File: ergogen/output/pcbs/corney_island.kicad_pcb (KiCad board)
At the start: 2 copper layers, 134 x 92.5 mm, 46 parts

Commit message: Add additional outputs: images, routed PCB, gerber
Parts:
- D1, D10, D11, D12, D13, D14, D15, D16, D17, D18, D19, D2, D20, D21, D3, D4, D5, D6, D7, D8, D9: value Nexperia_CFP3_SOD-123W -> (none); footprint Diode_SMD:Nexperia_CFP3_SOD-123W -> SmdDiode; moved to F.Cu
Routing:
- net ring_top: vias 0 -> 1
- net ring_home: vias 0 -> 1
- net ring_bottom: vias 0 -> 1
- net pinky_top: vias 0 -> 1
- net pinky_home: vias 0 -> 1
- net pinky_bottom: vias 0 -> 1
- net outer_top: vias 0 -> 1
- net outer_home: vias 0 -> 1
- net outer_bottom: vias 0 -> 1
- net near_home: vias 0 -> 1
- net middle_top: vias 0 -> 1
- net middle_home: vias 0 -> 2
- net middle_bottom: vias 0 -> 1
- net inner_top: vias 0 -> 1
- net inner_home: vias 0 -> 1
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
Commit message: Update outputs with additional plate files
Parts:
- D1, D10, D11, D12, D13, D14, D15, D16, D17, D18, D19, D2, D20, D21, D3, D4, D5, D6, D7, D8, D9: footprint SmdDiode -> ComboDiode
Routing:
- net ring_top: vias 1 -> 0
- net ring_home: vias 1 -> 0
- net ring_bottom: vias 1 -> 0
- net pinky_top: vias 1 -> 0
- net pinky_home: vias 1 -> 0
- net pinky_bottom: vias 1 -> 0
- net outer_top: vias 1 -> 0
- net outer_home: vias 1 -> 0
- net outer_bottom: vias 1 -> 0
- net near_home: vias 1 -> 0
- net middle_top: vias 1 -> 0
- net middle_home: vias 2 -> 0
- net middle_bottom: vias 1 -> 0
- net inner_top: vias 1 -> 0
- net inner_home: vias 1 -> 0
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
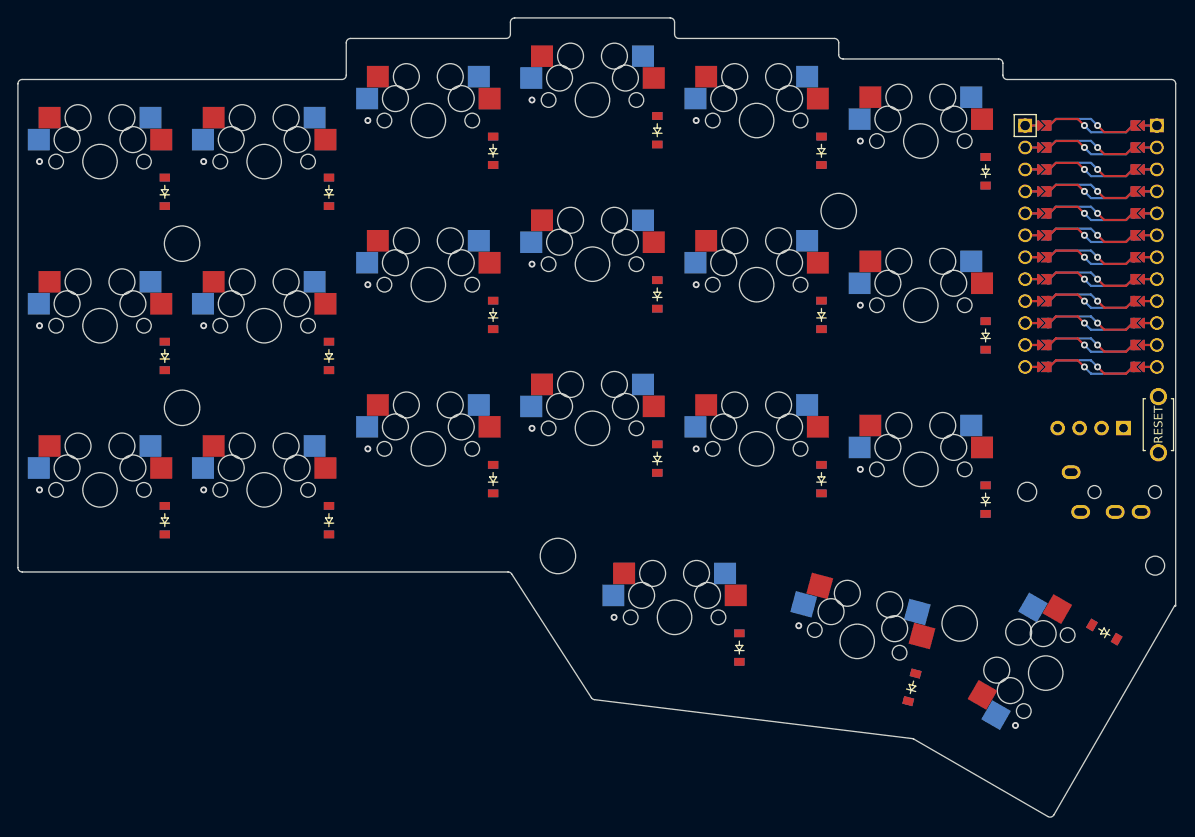
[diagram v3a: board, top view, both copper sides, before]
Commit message: Add LED cutouts
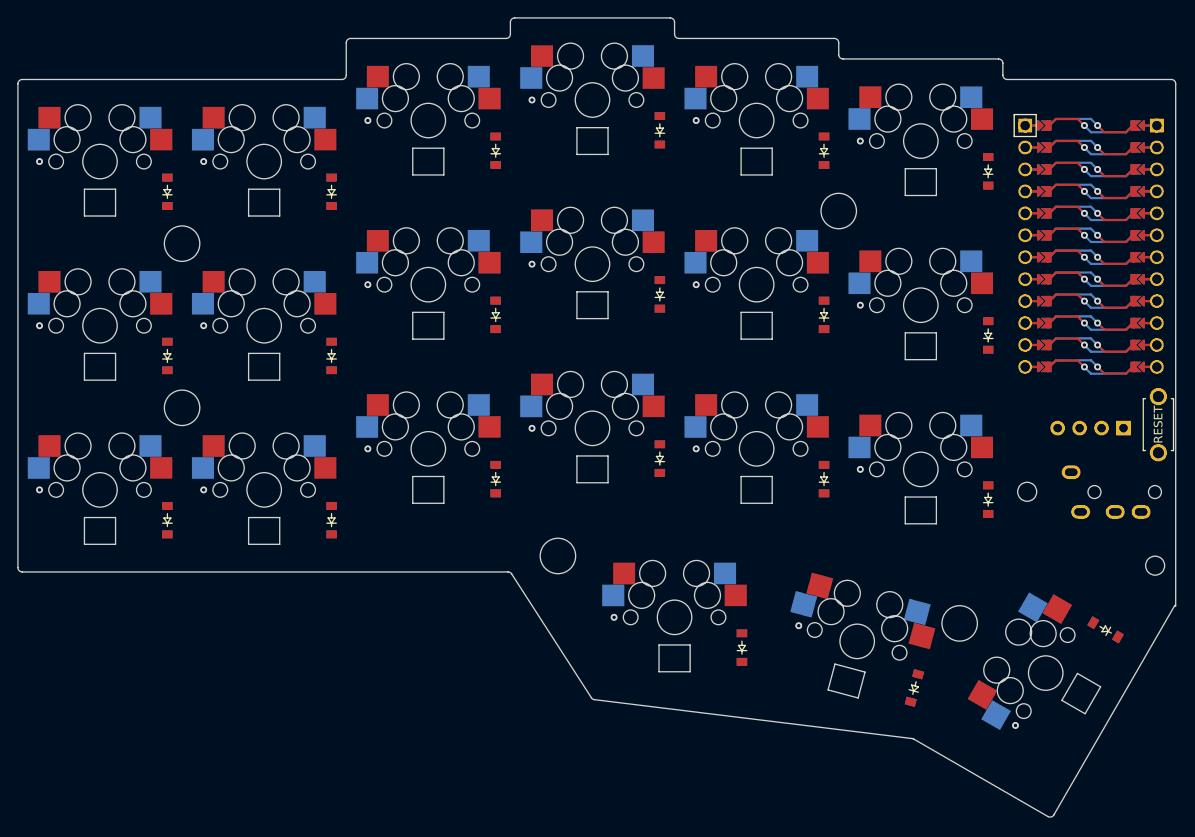
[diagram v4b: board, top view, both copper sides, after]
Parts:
- moved D20 0.30 mm to (194.3, 122.9)
- moved D10 0.30 mm to (164.8, 96.4)
- moved D11 0.30 mm to (164.8, 77.4)
- moved D12 0.30 mm to (164.8, 58.4)
- moved D13 0.30 mm to (183.8, 98.8)
- moved D14 0.30 mm to (183.8, 79.8)
- moved D15 0.30 mm to (183.8, 60.8)
- moved D16 0.30 mm to (202.8, 101.1)
- moved D17 0.30 mm to (202.8, 82.1)
- moved D18 0.30 mm to (202.8, 63.1)
- moved D19 0.30 mm to (174.3, 118.2)
- moved D7 0.30 mm to (145.8, 98.8)
- moved D8 0.30 mm to (145.8, 79.8)
- moved D9 0.30 mm to (145.8, 60.8)
- moved D1 0.30 mm to (107.8, 103.5)
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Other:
- outline, holes or cut-outs redrawn

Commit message: Fix key positions to exactly match the corne
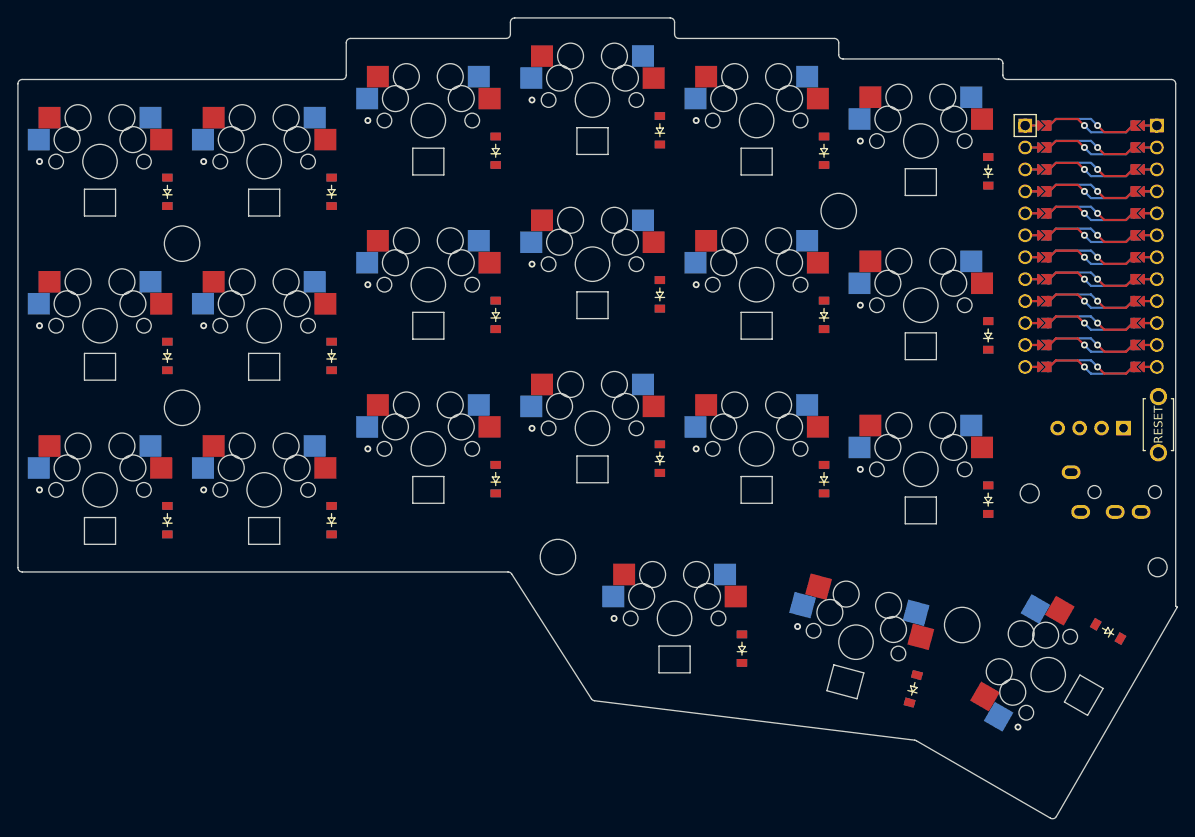
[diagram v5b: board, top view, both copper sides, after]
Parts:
- moved D21 0.34 mm to (216.7, 116.4)
- moved S21 0.34 mm to (209.7, 121.4)
- moved D20 0.16 mm to (194.1, 123.0)
- moved S20 0.16 mm to (187.5, 117.6)
- moved D19 0.12 mm to (174.3, 118.4)
- moved S19 0.12 mm to (166.5, 114.9)
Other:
- board size 134 x 92.5 mm -> 134.2 x 92.7 mm

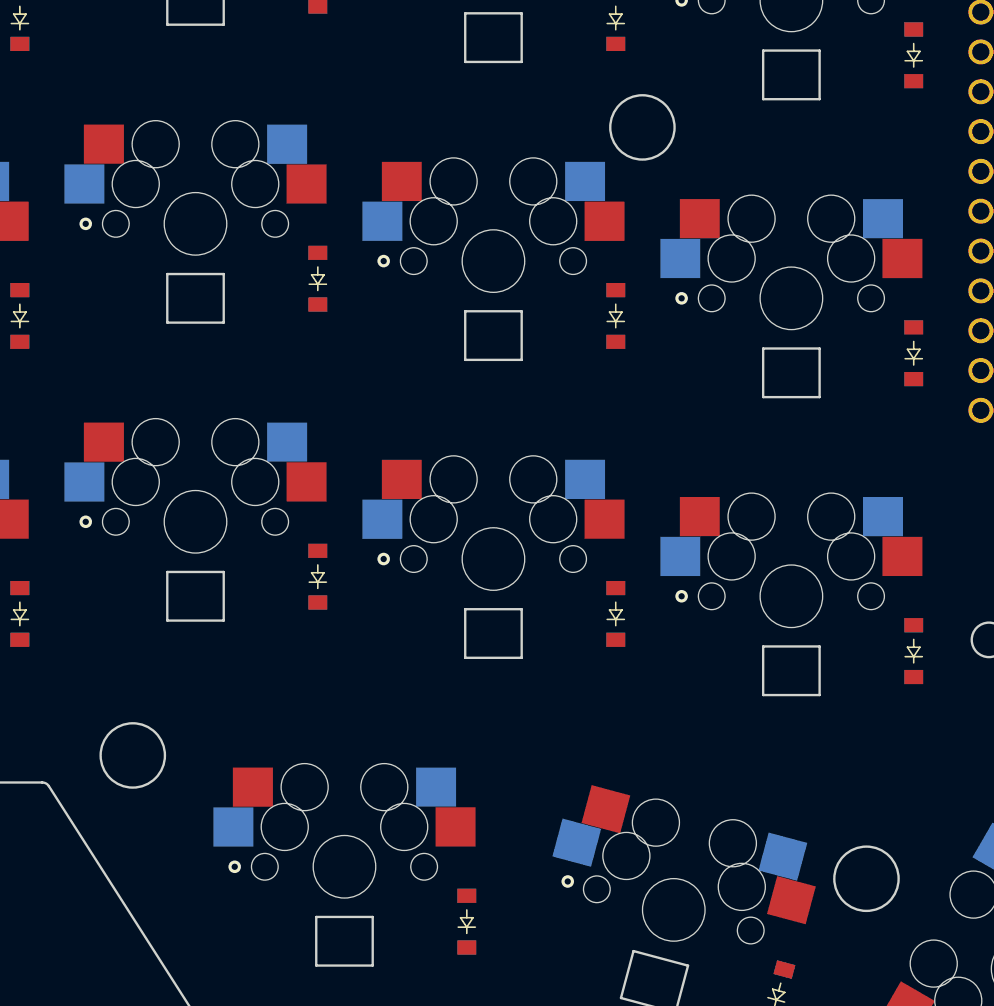
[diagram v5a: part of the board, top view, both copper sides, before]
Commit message: Fix screw spacer holes to match the corne
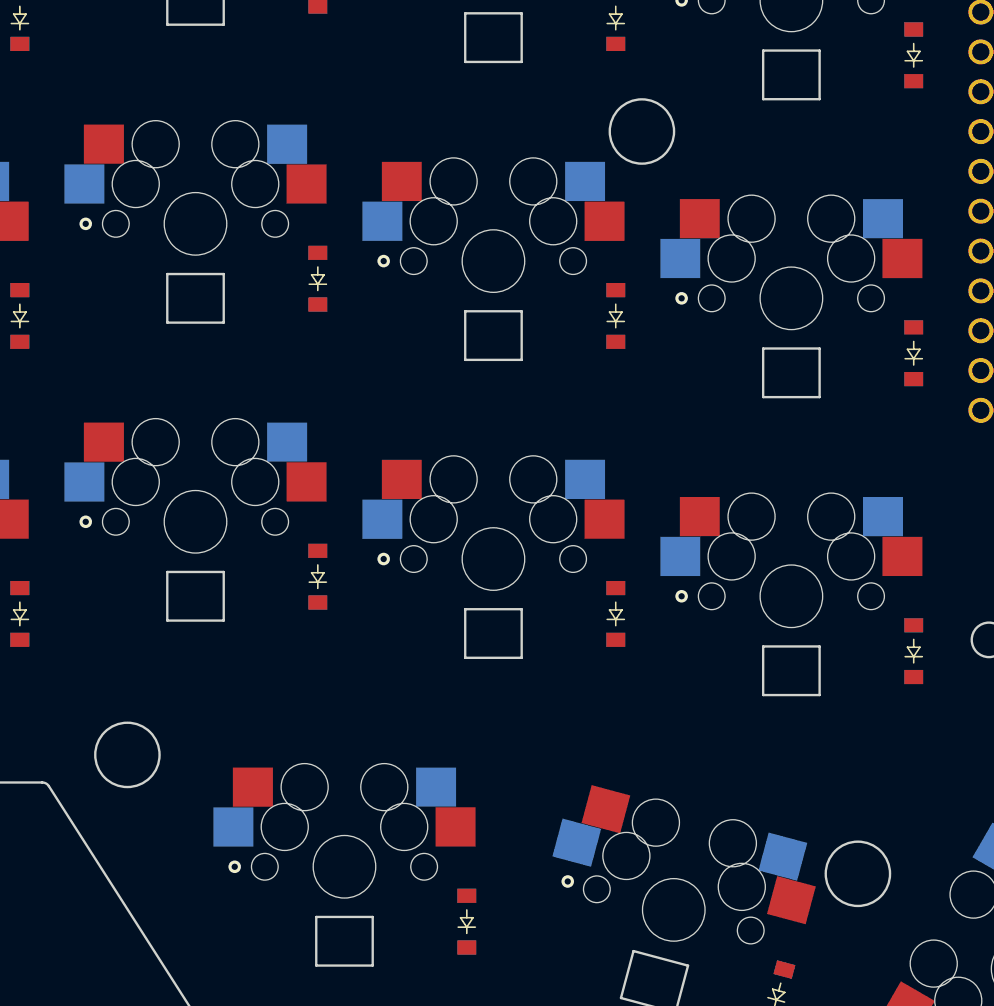
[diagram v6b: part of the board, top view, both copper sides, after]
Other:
- outline, holes or cut-outs redrawn
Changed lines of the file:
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@@
 (gr_circle (center 109.5 71.5) (end 111.55 71.5) (layer Edge.Cuts) (width 0.15))
 (gr_circle (center 109.5 90.5) (end 111.55 90.5) (layer Edge.Cuts) (width 0.15))
-(gr_circle (center 185.5 67.725) (end 187.55 67.725) (layer Edge.Cuts) (width 0.15))
-(gr_circle (center 153 107.775) (end 155.05 107.775) (layer Edge.Cuts) (width 0.15))
-(gr_circle (center 199.7875137 115.6391576) (end 201.83751370000002 115.6391576) (layer Edge.Cuts) (width 0.15))
+(gr_circle (center 185.468 67.986) (end 187.518 67.986) (layer Edge.Cuts) (width 0.15))
+(gr_circle (center 152.657 107.74) (end 154.70700000000002 107.74) (layer Edge.Cuts) (width 0.15))
+(gr_circle (center 199.2410516 115.3236576) (end 201.2910516 115.3236576) (layer Edge.Cuts) (width 0.15))
 (gr_circle (center 207.6013921 100.4051232) (end 208.7013921 100.4051232) (layer Edge.Cuts) (width 0.15))
 (gr_circle (center 222.4104265 108.9551232) (end 223.5104265 108.9551232) (layer Edge.Cuts) (width 0.15))

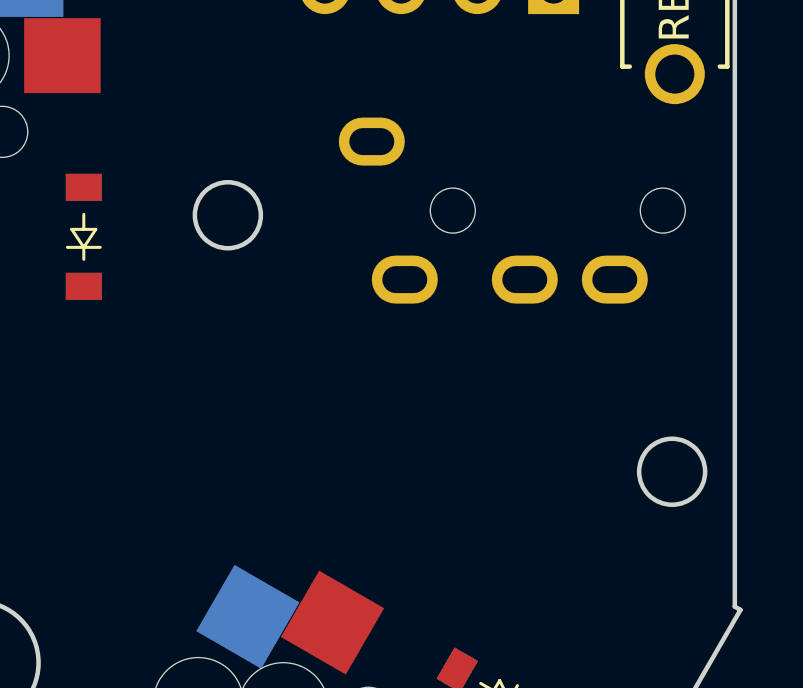
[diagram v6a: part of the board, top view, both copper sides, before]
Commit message: Fix MCU cover mounting holes position
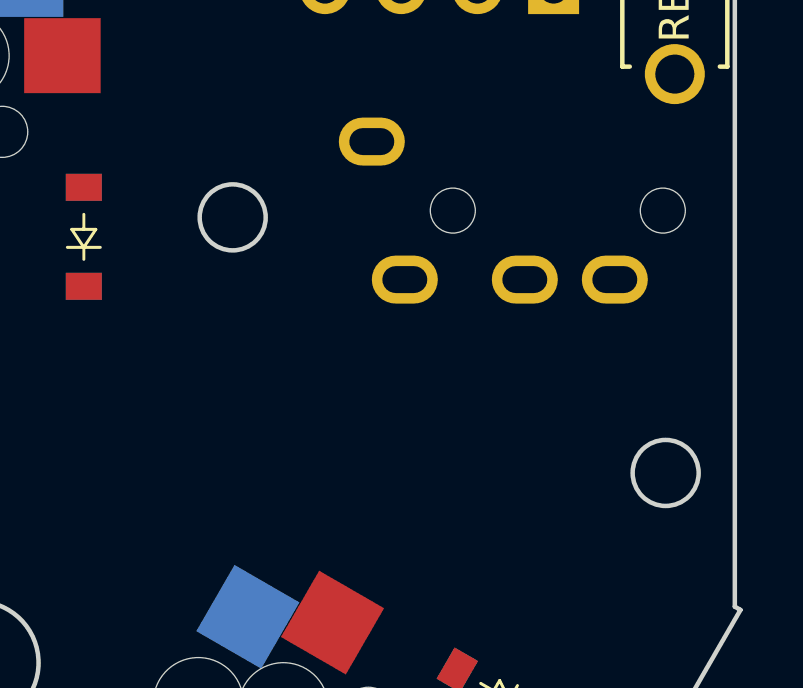
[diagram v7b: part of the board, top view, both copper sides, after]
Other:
- outline, holes or cut-outs redrawn
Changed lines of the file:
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@@
 (gr_circle (center 152.657 107.74) (end 154.70700000000002 107.74) (layer Edge.Cuts) (width 0.15))
 (gr_circle (center 199.2410516 115.3236576) (end 201.2910516 115.3236576) (layer Edge.Cuts) (width 0.15))
-(gr_circle (center 207.6013921 100.4051232) (end 208.7013921 100.4051232) (layer Edge.Cuts) (width 0.15))
-(gr_circle (center 222.4104265 108.9551232) (end 223.5104265 108.9551232) (layer Edge.Cuts) (width 0.15))
+(gr_circle (center 207.762 100.476) (end 208.862 100.476) (layer Edge.Cuts) (width 0.15))
+(gr_circle (center 222.194 108.995) (end 223.29399999999998 108.995) (layer Edge.Cuts) (width 0.15))
 (gr_line (start 98.2 106.3) (end 101.8 106.3) (angle 90) (layer Edge.Cuts) (width 0.15))
 (gr_line (start 101.8 106.3) (end 101.8 103.2) (angle 90) (layer Edge.Cuts) (width 0.15))

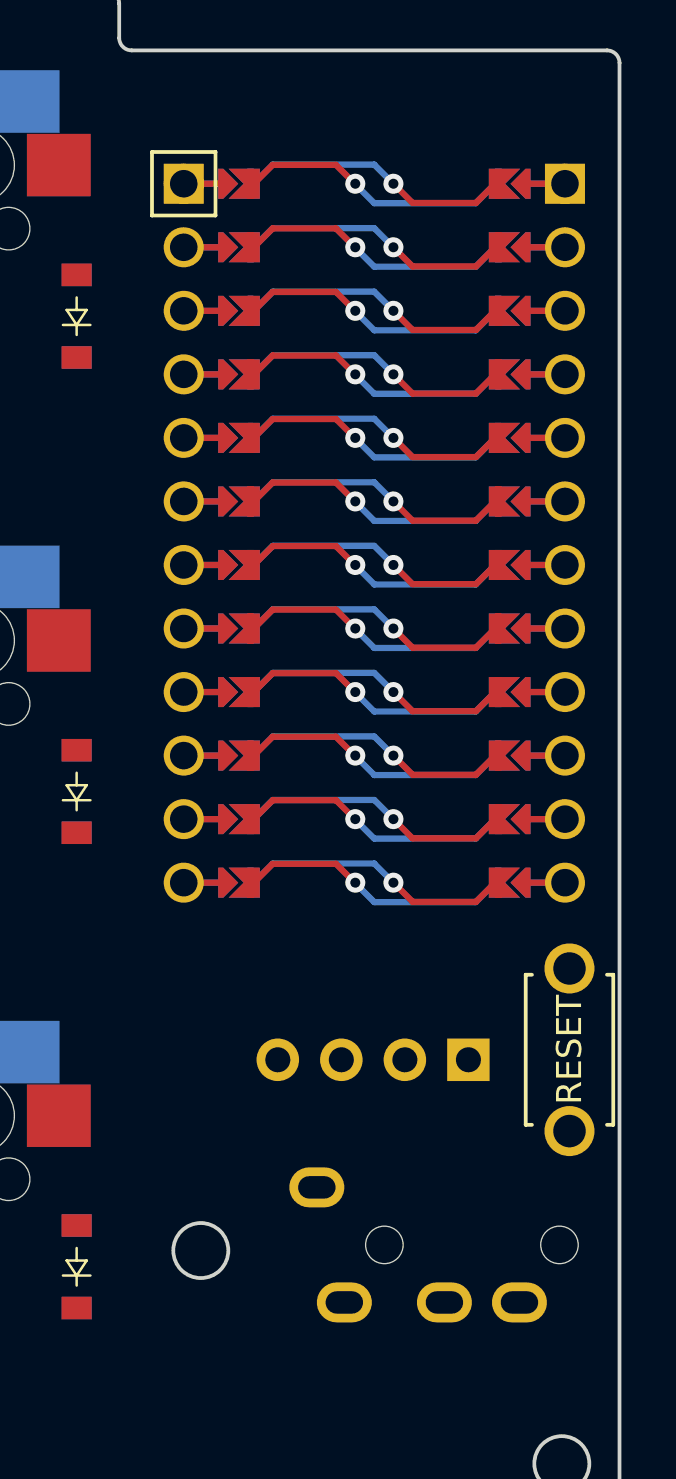
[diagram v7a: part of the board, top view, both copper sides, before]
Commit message: Fix component positions to match the corne
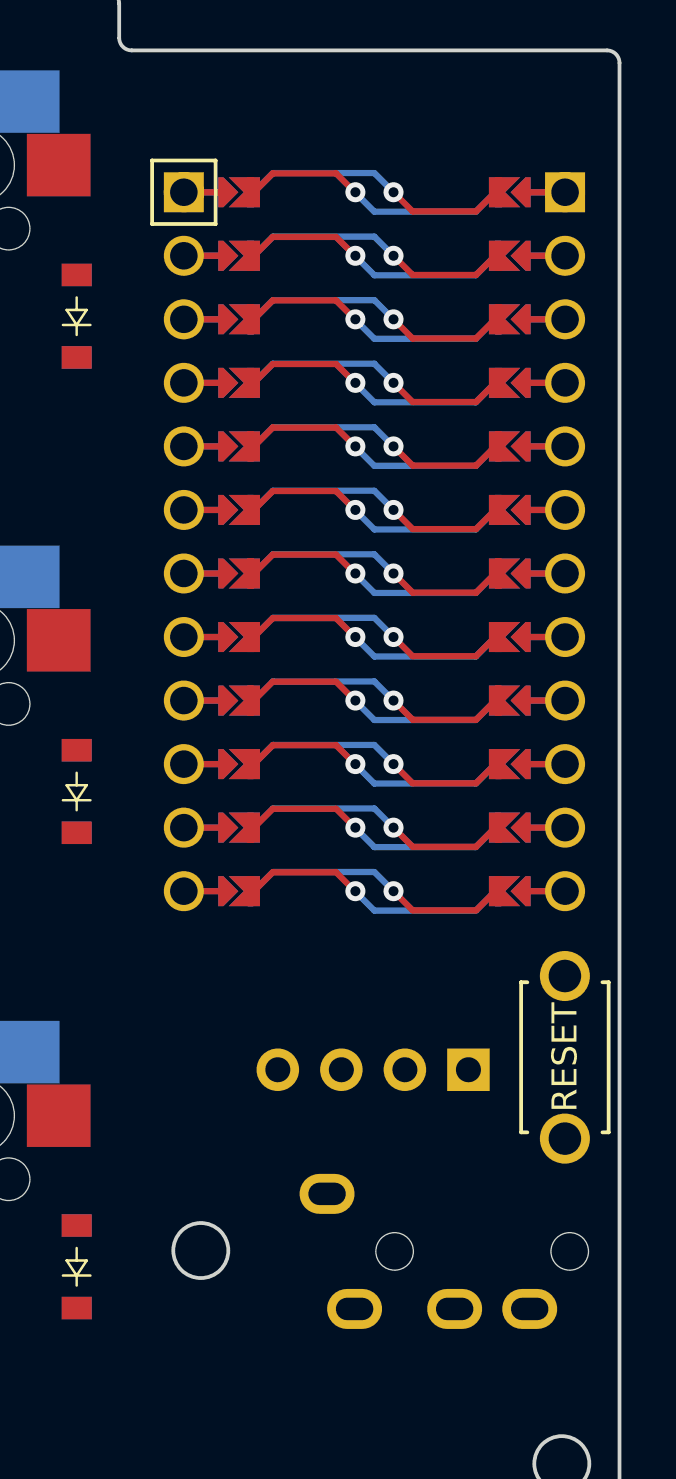
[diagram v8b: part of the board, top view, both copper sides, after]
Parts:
- moved TRRS1 0.49 mm to (224.1, 102.8)
- moved OLED1 0.40 mm to (208.7, 94.8)
- moved B1 0.35 mm to (222.3, 92.8)
- moved MCU1 0.34 mm to (214.7, 72.1)
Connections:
- B1 pad 1: GND -> RST
- B1 pad 2: RST -> GND
